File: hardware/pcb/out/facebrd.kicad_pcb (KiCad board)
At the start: 2 copper layers, 56 x 68 mm, 33 parts, among them J1 ToF 4P, J2 MIC pads, J3 EYES 6P, J4 BAT, J5 LED 3P, J6 AMP 5P, J7 TOUCH pads, J8 CHG, U1 XIAO-ESP32S3, U2 MPR121QR2, U3 MPU-6050

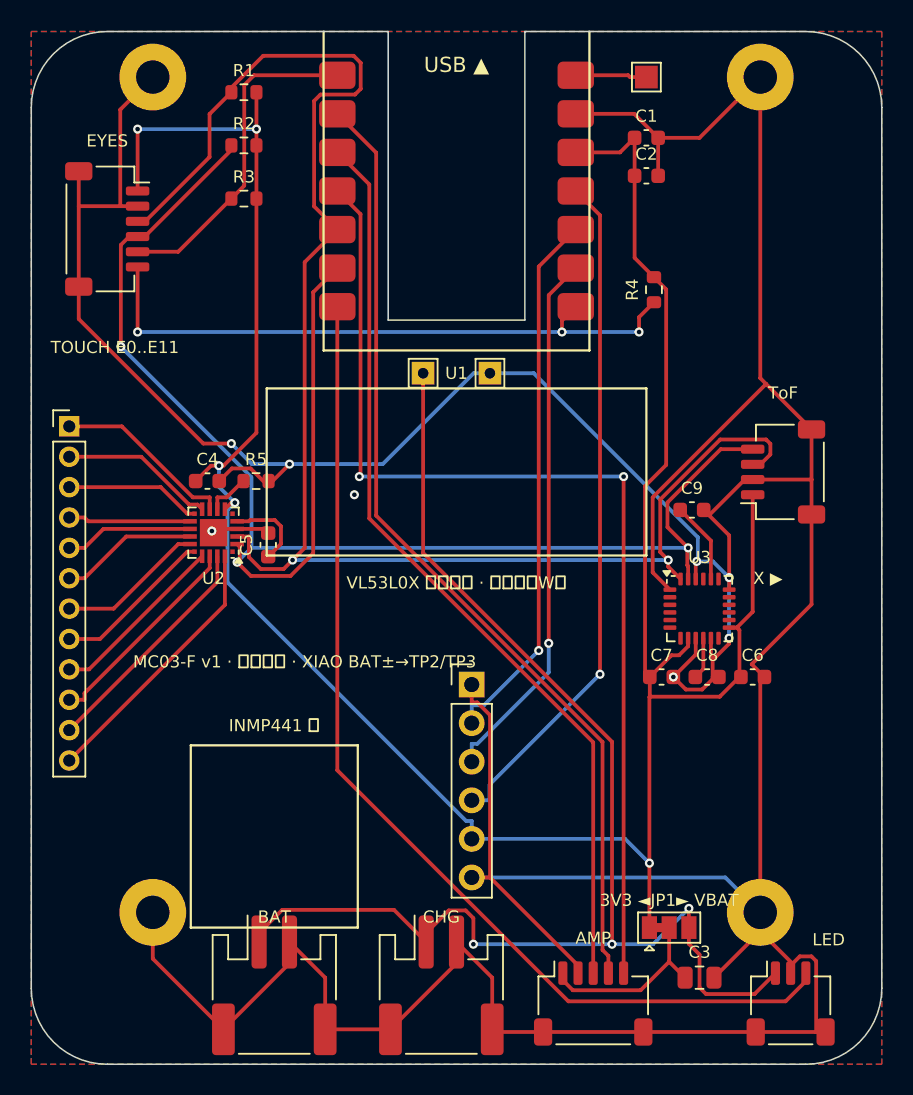
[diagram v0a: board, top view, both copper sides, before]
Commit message: pcb: MC03-F re-layout by XIAO pin side, back-side GND plane only; fixed W/M cells for all creatures
Co-Authored-By: Claude Fable 5.1 <noreply@anthropic.com>
Claude-Session: https://claude.ai/code/session_01F351BE8WNbsDJxZJegnrAN
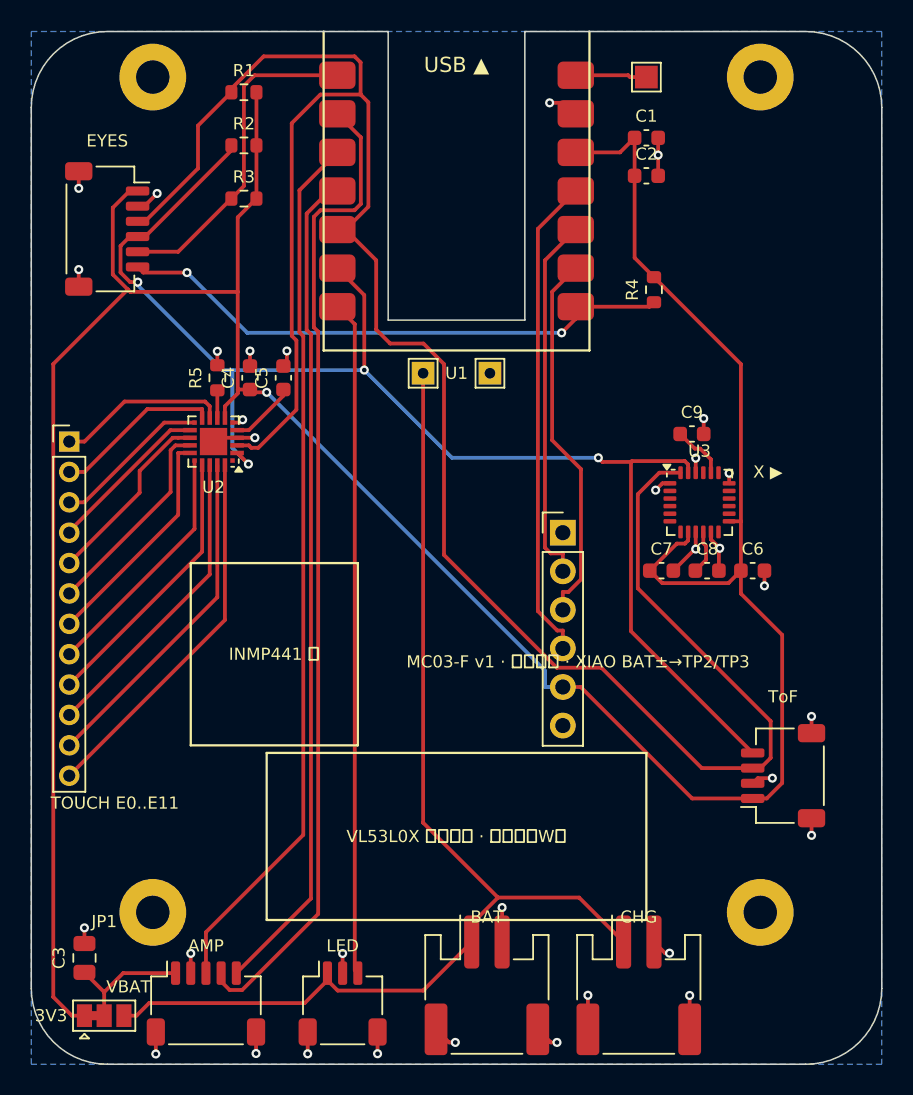
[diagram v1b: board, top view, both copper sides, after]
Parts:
- moved C3 40.5 mm to (-24.5, 26.0), turned to 90 degrees
- moved JP1 37.6 mm to (-23.2, 29.8)
- moved J5 29.5 mm to (-7.50, 29.0)
- moved J6 25.5 mm to (-16.5, 29.0)
- moved J1 20.0 mm to (21.5, 14.0)
- moved J4 14.0 mm to (2.00, 27.8)
- moved J8 13.0 mm to (12.0, 27.8)
- moved J2 11.7 mm to (7.00, -2.00)
- moved C5 11.0 mm to (-11.4, -12.2)
- moved C4 7.35 mm to (-13.6, -12.2), turned to 90 degrees
- moved R5 7.26 mm to (-15.8, -12.2), turned to 90 degrees
- moved C6 7.00 mm to (19.5, 0.50)
- moved C7 7.00 mm to (13.5, 0.50)
- moved C8 7.00 mm to (16.5, 0.50)
- moved U3 7.00 mm to (16.0, -4.00)
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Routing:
- net GND: track 334.9 -> 50.1 mm, vias 8 -> 33
- net SDA0: track 105.7 -> 140.2 mm, vias 2 -> 0
- net 3V3: track 166.2 -> 198.9 mm, vias 5 -> 1
- net LED_DIN: track 68.8 -> 44.4 mm
- net I2S_DIN: track 69.6 -> 54.8 mm, vias 2 -> 0
- net MIC_SD: track 45.0 -> 32.0 mm, vias 1 -> 0
- net VBAT: track 88.5 -> 75.6 mm, vias 3 -> 0
- net MIC_WS: track 35.8 -> 24.3 mm, vias 1 -> 0
- net MIC_SCK: track 35.6 -> 24.6 mm, vias 1 -> 0
- net SCL0: track 103.3 -> 92.9 mm, vias 3 -> 4
- net ELE10: track 15.5 -> 22.5 mm
- net ELE11: track 17.7 -> 24.7 mm
- net ELE9: track 13.9 -> 20.3 mm
- net ELE8: track 11.8 -> 18.1 mm
- net ELE7: track 10.6 -> 16.2 mm
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- removed copper zone on F.Cu, net GND
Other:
- board text added: "3V3"
- board text added: "JP1"
- board text added: "VBAT"
- board text removed: "3V3 ◄JP1► VBAT"

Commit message: pcb: JLCPCB order-number placeholder on the back silkscreen
Co-Authored-By: Claude Fable 5.1 <noreply@anthropic.com>
Claude-Session: https://claude.ai/code/session_01F351BE8WNbsDJxZJegnrAN
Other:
- board text added: "JLCJLCJLCJLC"
